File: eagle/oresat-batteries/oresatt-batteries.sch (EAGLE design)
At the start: 7 parts, among them U1 TCAN330

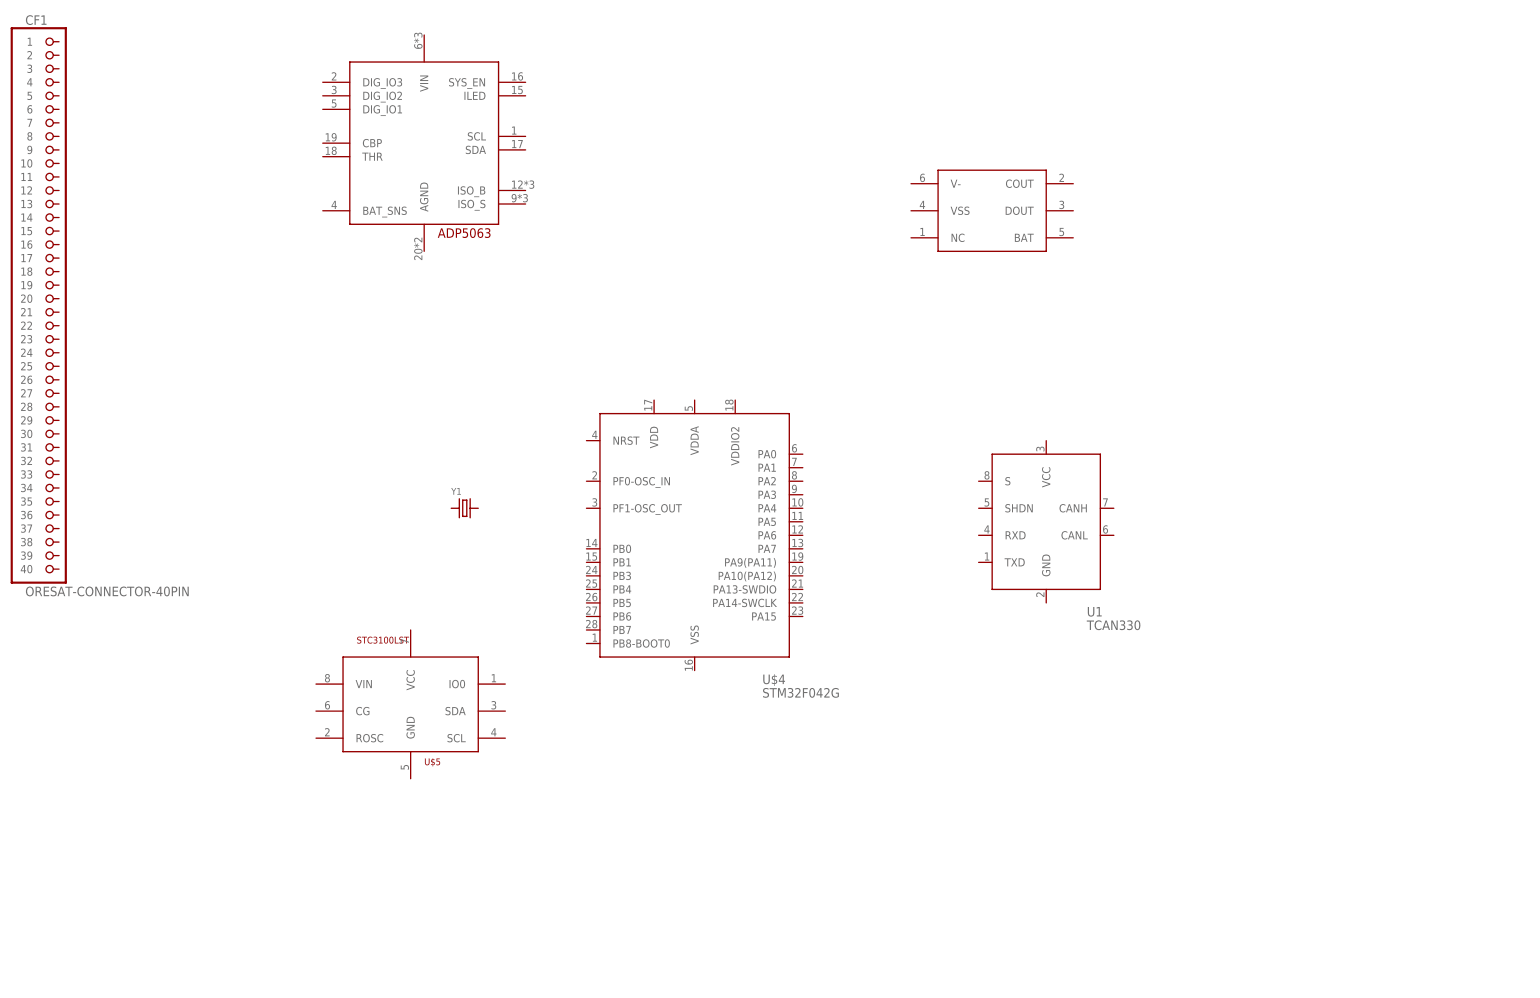
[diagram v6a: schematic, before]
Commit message: Added potential battery to schematic
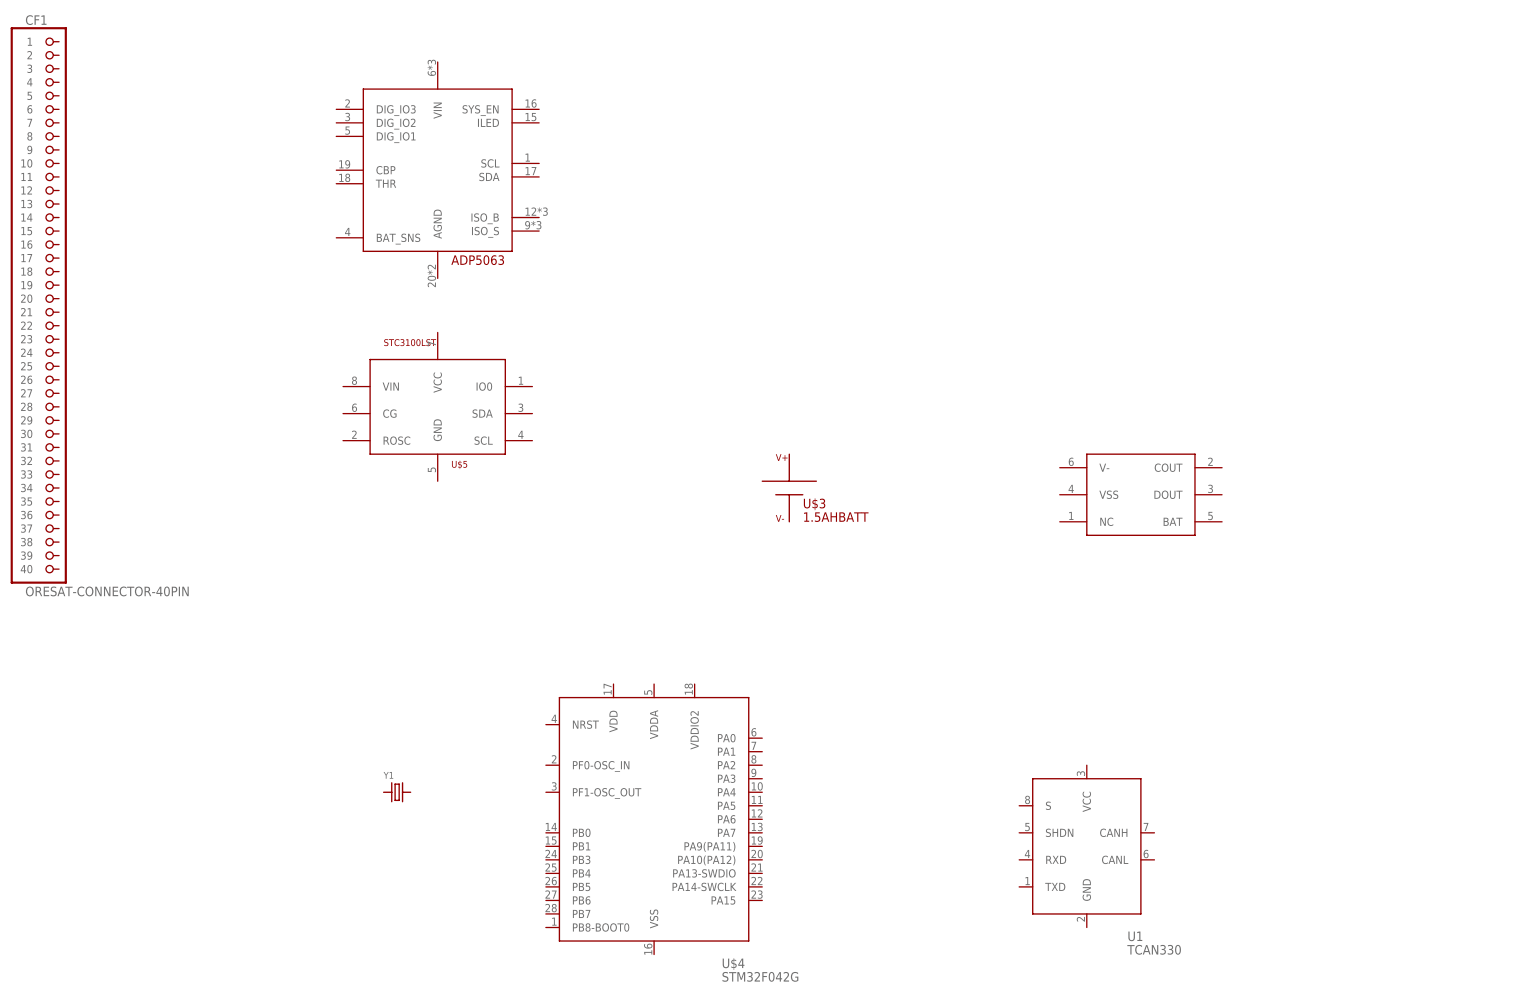
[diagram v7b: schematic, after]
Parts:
- added U$3: 1.5AHBATT, oresat-batteries:1.5AHBATT
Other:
- moved on the sheet: U$4, U$5, U1, Y1
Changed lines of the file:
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@@
 <part name="CF1" library="low-gain-radio" deviceset="ORESAT-CONNECTOR-40PIN" device=""/>
 <part name="U$5" library="oresat-batteries" deviceset="STC3100LST" device=""/>
+<part name="U$3" library="oresat-batteries" deviceset="1.5AHBATT" device=""/>
 </parts>
 <sheets>
@@
 </plain>
 <instances>
-<instance part="U$1" gate="G$1" x="-81.28" y="30.48"/>
-<instance part="U$2" gate="G$1" x="25.4" y="17.78"/>
-<instance part="U$4" gate="G$1" x="-30.48" y="-43.18"/>
-<instance part="U1" gate="G$1" x="35.56" y="-40.64"/>
-<instance part="Y1" gate="G$1" x="-73.66" y="-38.1"/>
+<instance part="U$1" gate="G$1" x="-78.74" y="25.4"/>
+<instance part="U$2" gate="G$1" x="53.34" y="-35.56"/>
+<instance part="U$4" gate="G$1" x="-38.1" y="-96.52"/>
+<instance part="U1" gate="G$1" x="43.18" y="-101.6"/>
+<instance part="Y1" gate="G$1" x="-86.36" y="-91.44"/>
 <instance part="CF1" gate="G$1" x="-149.86" y="0"/>
-<instance part="U$5" gate="G$1" x="-83.82" y="-73.66"/>
+<instance part="U$5" gate="G$1" x="-78.74" y="-17.78"/>
+<instance part="U$3" gate="G$1" x="-12.7" y="-35.56"/>
 </instances>
 <busses>

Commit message: Started rough layout of boards. Updated design docs (see google docs)
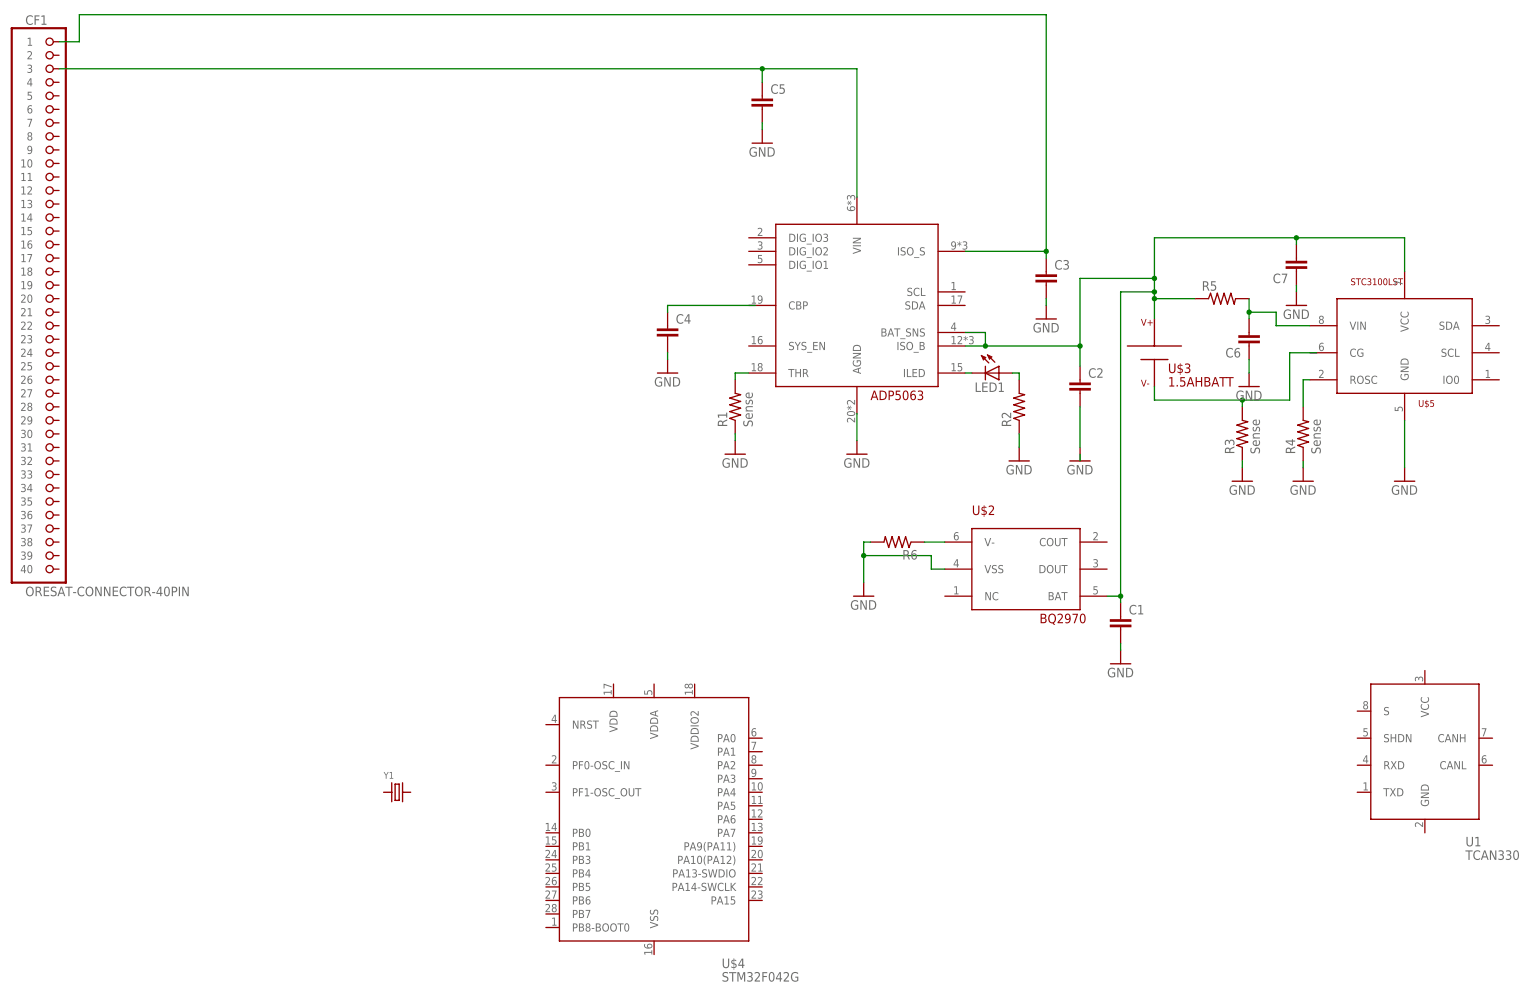
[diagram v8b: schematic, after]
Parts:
- added C1, C2, C3, C4, C5, C6, C7: (no value), rcl:C-EUC0603
- added LED1: (no value), led:LEDCHIPLED_0603
- added R1, R3, R4: Sense, rcl:R-US_R0603
- added R2, R5, R6: (no value), rcl:R-US_R0603
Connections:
- new net GND: C1.2, C2.2, C3.2, C4.2, C5.2, C6.1, C7.1, R1.1, R2.1, R3.1, R4.1, R6.2, U$1.AGND, U$2.VSS, U$5.GND
- new net N$1: R1.2, U$1.THR
- new net N$10: R6.1, U$2.V-
- new net N$2: LED1.A, R2.2
- new net N$3: LED1.C, U$1.ILED
- new net N$4: C3.1, CF1.1, U$1.ISO_S
- new net N$5: C5.1, CF1.3, U$1.VIN
- new net N$6: C4.1
- new net N$7: R4.2, U$5.ROSC
- new net N$8: R3.2
- new net N$9: C6.2, R5.2, U$5.VIN
- new net VBAT+: C1.1, C2.1, C7.2, R5.1, U$1.BAT_SNS, U$1.ISO_B, U$2.BAT, U$5.VCC
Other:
- moved on the sheet: U$3, U$5, U1
